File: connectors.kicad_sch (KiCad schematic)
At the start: 0 parts

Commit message: Add RS485 transciever
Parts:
- added J1: 112-024-113R001, Connector_Centronics:CONN_112-024-113R001_NRC, symbol PARTSDB:112-024-113R001
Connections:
- new net GND: J1.18 (Pin_18), J1.19 (Pin_19), J1.20 (Pin_20), J1.21 (Pin_21), J1.22 (Pin_22), J1.23 (Pin_23), J1.24 (Pin_24)

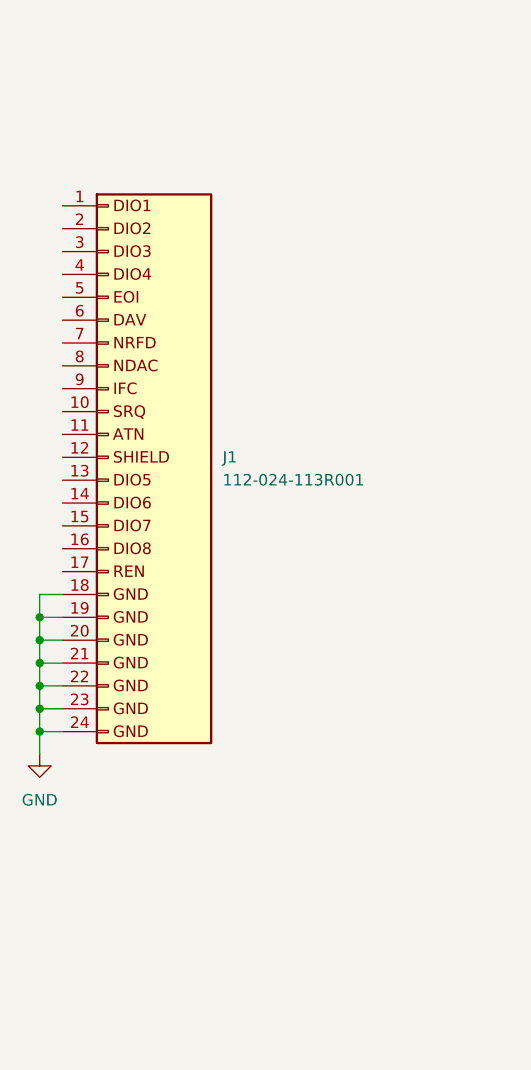
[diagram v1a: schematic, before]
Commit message: Add GPIB and RS485 (CtrlLink) ports
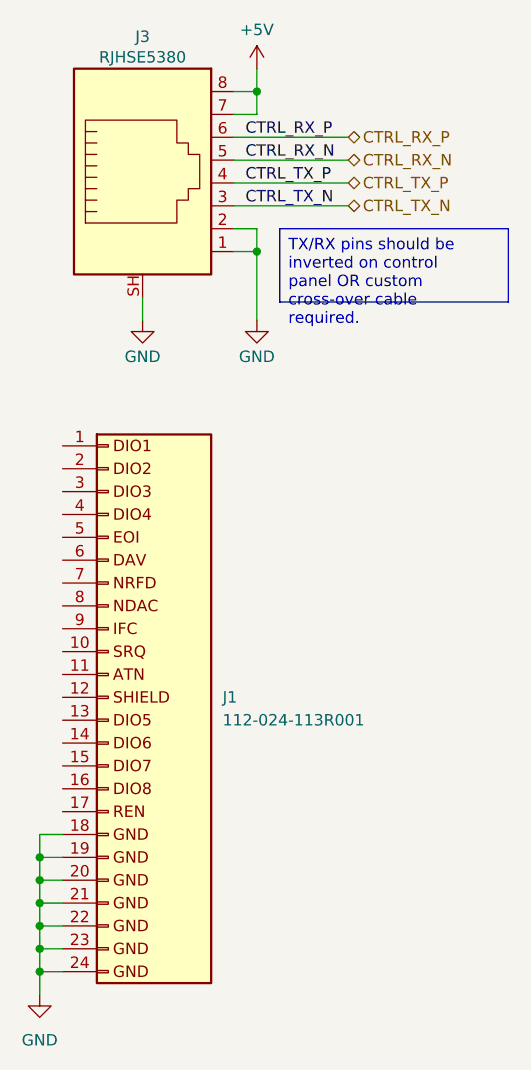
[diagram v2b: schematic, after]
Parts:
- added J3: RJHSE5380, Connector_RJ:RJ45_Amphenol_RJHSE5380, symbol PARTSDB:RJHSE5380
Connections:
- net GND: now also J3.1, J3.2, J3.SH
- new net +5V: J3.7, J3.8
- new net CTRL_RX_N: J3.5
- new net CTRL_RX_P: J3.6
- new net CTRL_TX_N: J3.3
- new net CTRL_TX_P: J3.4
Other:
- moved on the sheet: J1

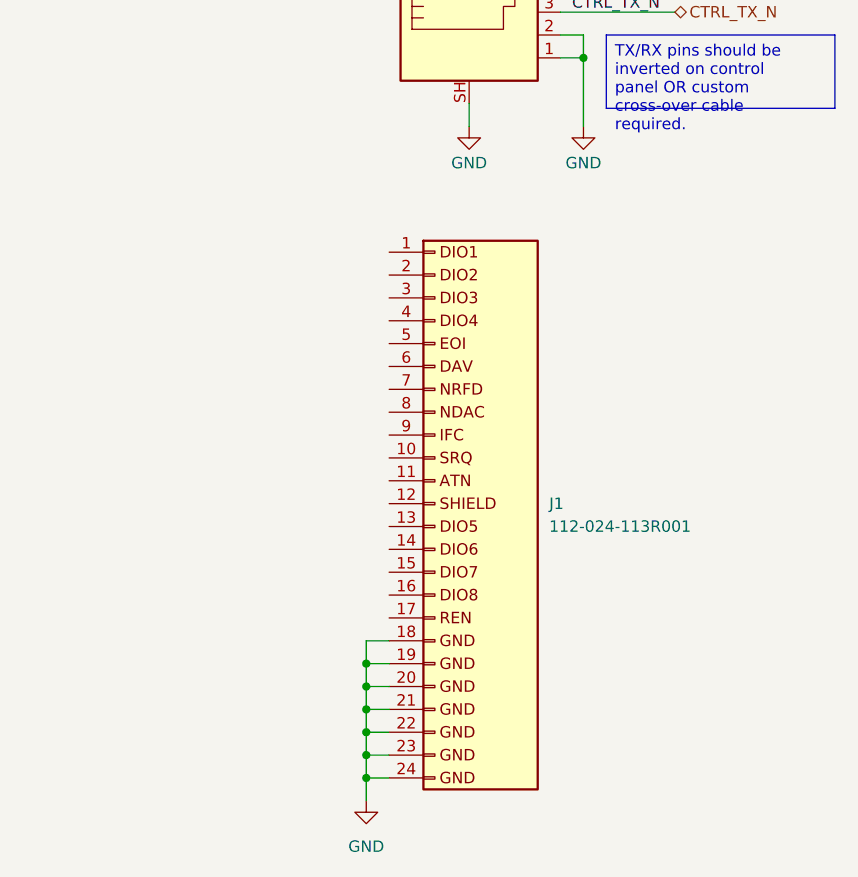
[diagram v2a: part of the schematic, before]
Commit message: Link DIO nets to GPIB connector
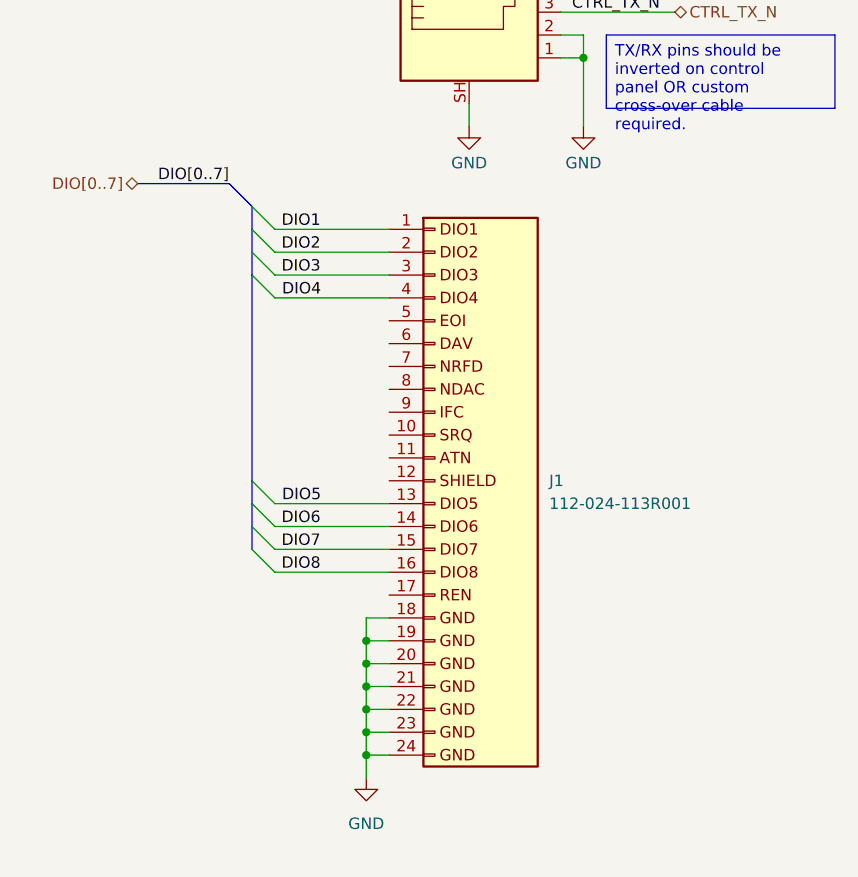
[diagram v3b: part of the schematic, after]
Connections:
- net DIO1: now reaches J1.1 (Pin_1)
- net DIO6: now reaches J1.14 (Pin_14)
- net DIO7: now reaches J1.15 (Pin_15)
- net DIO8: now reaches J1.16 (Pin_16)
- net DIO2: now reaches J1.2 (Pin_2)
- net DIO3: now reaches J1.3 (Pin_3)
- net DIO4: now reaches J1.4 (Pin_4)
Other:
- moved on the sheet: J1

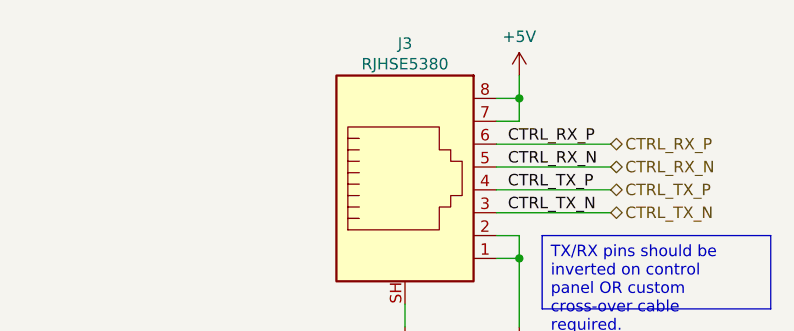
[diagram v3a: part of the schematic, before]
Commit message: Added open-drain driver for GPIB control pins
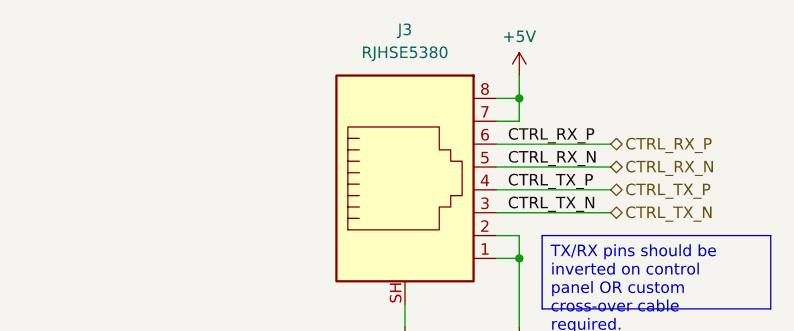
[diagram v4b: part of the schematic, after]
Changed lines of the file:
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@@
+	)
+	(symbol
+		(lib_id "PARTSDB:RJHSE5380")
+		(at 190.5 60.96 0)
+		(unit 1)
+		(body_style 1)
+		(exclude_from_sim no)
+		(in_bom yes)
+		(on_board yes)
+		(in_pos_files yes)
+		(dnp no)
+		(fields_autoplaced yes)
+		(property "Reference" "J3"
+			(at 190.5 43.18 0)
+			(show_name no)
+			(do_not_autoplace no)
+			(effects
+				(font
+					(size 1.27 1.27)
+				)
+			)
+		)
+		(property "Value" "RJHSE5380"
+			(at 190.5 45.72 0)
+			(show_name no)
+			(do_not_autoplace no)
+			(effects
+				(font
+					(size 1.27 1.27)
+				)
+			)
+		)
+		(property "Footprint" "Connector_RJ:RJ45_Amphenol_RJHSE5380"
+			(at 190.5 60.325 90)
+			(hide yes)
+			(show_name no)
+			(do_not_autoplace no)
+			(effects
+				(font
+					(size 1.27 1.27)
+				)
+			)
+		)
+		(property "Datasheet" "https://cdn.amphenol-cs.com/media/wysiwyg/files/documentation/datasheet/inputoutput/io-modjack-rjhse.pdf"
+			(at 190.5 60.325 90)
+			(hide yes)
+			(show_name no)
+			(do_not_autoplace no)
+			(effects
+				(font
+					(size 1.27 1.27)
+				)
+			)
+		)
+		(property "Description" "Jack Modular Connector 8p8c (RJ45, Ethernet) 90° Angle (Right) Shielded, EMI Finger"
+			(at 190.5 60.96 0)
+			(hide yes)
+			(show_name no)
+			(do_not_autoplace no)
+			(effects
+				(font
+					(size 1.27 1.27)
+				)
+			)
+		)
+		(property "Part-DB URL" "http://parts.husbylabs.com/en/part/12/info"
+			(at 190.5 60.96 0)
+			(hide yes)
+			(show_name no)
+			(do_not_autoplace no)
+			(effects
+				(font
+					(size 1.27 1.27)
+				)
+			)
+		)
+		(property "Category" "Connectors, Interconnects/Modular/Ethernet Connectors"
+			(at 190.5 60.96 0)
+			(hide yes)
+			(show_name no)
+			(do_not_autoplace no)
+			(effects
+				(font
+					(size 1.27 1.27)
+				)
+			)
+		)
+		(property "Manufacturer" "Amphenol ICC (Commercial Products)"
+			(at 190.5 60.96 0)
+			(hide yes)
+			(show_name no)
+			(do_not_autoplace no)
+			(effects
+				(font
+					(size 1.27 1.27)
+				)
+			)
+		)
+		(property "MPN" "RJHSE5380"
+			(at 190.5 60.96 0)
+			(hide yes)
+			(show_name no)
+			(do_not_autoplace no)
+			(effects
+				(font
+					(size 1.27 1.27)
+				)
+			)
+		)
+		(property "Manufacturing Status" "Active"
+			(at 190.5 60.96 0)
+			(hide yes)
+			(show_name no)
+			(do_not_autoplace no)
+			(effects
+				(font
+					(size 1.27 1.27)
+				)
+			)
+		)
+		(property "Part-DB ID" "12"
+			(at 190.5 60.96 0)
+			(hide yes)
+			(show_name no)
+			(do_not_autoplace no)
+			(effects
+				(font
+					(size 1.27 1.27)
+				)
+			)
+		)
+		(property "manf" "Amphenol ICC (Commercial Products)"
+			(at 190.5 60.96 0)
+			(hide yes)
+			(show_name no)
+			(do_not_autoplace no)
+			(effects
+				(font
+					(size 1.27 1.27)
+				)
+			)
+		)
+		(property "manf#" "RJHSE5380"
+			(at 190.5 60.96 0)
+			(hide yes)
+			(show_name no)
+			(do_not_autoplace no)
+			(effects
+				(font
+					(size 1.27 1.27)
+				)
+			)
+		)
+		(property "DigiKey SPN" "664-RJHSE5380-ND"
+			(at 190.5 60.96 0)
+			(hide yes)
+			(show_name no)
+			(do_not_autoplace no)
+			(effects
+				(font
+					(size 1.27 1.27)
+				)
+			)
+		)
+		(property "digikey#" "664-RJHSE5380-ND"
+			(at 190.5 60.96 0)
+			(hide yes)
+			(show_name no)
+			(do_not_autoplace no)
+			(effects
+				(font
+					(size 1.27 1.27)
+				)
+			)
+		)
+		(property "Stock" "0"
+			(at 190.5 60.96 0)
+			(hide yes)
+			(show_name no)
+			(do_not_autoplace no)
+			(effects
+				(font
+					(size 1.27 1.27)
+				)
+			)
+		)
+		(pin "7"
+		)
+		(pin "8"
+		)
+		(pin "SH"
+		)
+		(pin "6"
+		)
+		(pin "1"
+		)
+		(pin "2"
+		)
+		(pin "3"
+		)
+		(pin "4"
+		)
+		(pin "5"
+		)
+		(instances
+			(project "gpib_controller"
+				(path "/0f352524-50ff-469d-9a68-783e183b0073/642cbd6b-8c2c-4a8a-b65c-89c798f24c3f/b8b9e038-f19a-4634-b386-ca56990adcb1"
+					(reference "J3")
+					(unit 1)
+				)
+			)
+		)
 	)
 	(symbol
@@
 					(unit 1)
 				)
-			)
-		)
-	)
-	(symbol
-		(lib_id "PARTSDB:RJHSE5380")
-		(at 190.5 60.96 0)
-		(unit 1)
-		(body_style 1)
-		(exclude_from_sim no)
-		(in_bom yes)
-		(on_board yes)
-		(in_pos_files yes)
-		(dnp no)
-		(property "Reference" "J3"
-			(at 190.5 44.704 0)
-			(show_name no)
-			(do_not_autoplace no)
-			(effects
-				(font
-					(size 1.27 1.27)
-				)
-			)
-		)
-		(property "Value" "RJHSE5380"
-			(at 190.5 46.99 0)
-			(show_name no)
-			(do_not_autoplace no)
-			(effects
-				(font
-					(size 1.27 1.27)
-				)
-			)
-		)
-		(property "Footprint" "Connector_RJ:RJ45_Amphenol_RJHSE5380"
-			(at 190.5 60.325 90)
-			(hide yes)
-			(show_name no)
-			(do_not_autoplace no)
-			(effects
-				(font
-					(size 1.27 1.27)
-				)
-			)
-		)
-		(property "Datasheet" "https://cdn.amphenol-cs.com/media/wysiwyg/files/documentation/datasheet/inputoutput/io-modjack-rjhse.pdf"
-			(at 190.5 60.325 90)
-			(hide yes)
-			(show_name no)
-			(do_not_autoplace no)
-			(effects
-				(font
-					(size 1.27 1.27)
-				)
-			)
-		)
-		(property "Description" "Jack Modular Connector 8p8c (RJ45, Ethernet) 90° Angle (Right) Shielded, EMI Finger"
-			(at 190.5 60.96 0)
-			(hide yes)
-			(show_name no)
-			(do_not_autoplace no)
-			(effects
-				(font
-					(size 1.27 1.27)
-				)
-			)
-		)
-		(property "Part-DB URL" "http://parts.husbylabs.com/en/part/12/info"
-			(at 190.5 60.96 0)
-			(hide yes)
-			(show_name no)
-			(do_not_autoplace no)
-			(effects
-				(font
-					(size 1.27 1.27)
-				)
-			)
-		)
-		(property "Category" "Connectors, Interconnects/Modular/Ethernet Connectors"
-			(at 190.5 60.96 0)
-			(hide yes)
-			(show_name no)
-			(do_not_autoplace no)
-			(effects
-				(font
-					(size 1.27 1.27)
-				)
-			)
-		)
-		(property "Manufacturer" "Amphenol ICC (Commercial Products)"
-			(at 190.5 60.96 0)
-			(hide yes)
-			(show_name no)
-			(do_not_autoplace no)
-			(effects
-				(font
-					(size 1.27 1.27)
-				)
-			)
-		)
-		(property "MPN" "RJHSE5380"
-			(at 190.5 60.96 0)
-			(hide yes)
-			(show_name no)
-			(do_not_autoplace no)
-			(effects
-				(font
-					(size 1.27 1.27)
-				)
-			)
-		)
-		(property "Manufacturing Status" "Active"
-			(at 190.5 60.96 0)
-			(hide yes)
-			(show_name no)
-			(do_not_autoplace no)
-			(effects
-				(font
-					(size 1.27 1.27)
-				)
-			)
-		)
-		(property "Part-DB ID" "12"
-			(at 190.5 60.96 0)
-			(hide yes)
-			(show_name no)
-			(do_not_autoplace no)
-			(effects
-				(font
-					(size 1.27 1.27)
-				)
-			)
-		)
-		(property "manf" "Amphenol ICC (Commercial Products)"
-			(at 190.5 60.96 0)
-			(hide yes)
-			(show_name no)
-			(do_not_autoplace no)
-			(effects
-				(font
-					(size 1.27 1.27)
-				)
-			)
-		)
-		(property "manf#" "RJHSE5380"
-			(at 190.5 60.96 0)
-			(hide yes)
-			(show_name no)
-			(do_not_autoplace no)
-			(effects
-				(font
-					(size 1.27 1.27)
-				)
-			)
-		)
-		(property "DigiKey SPN" "664-RJHSE5380-ND"
-			(at 190.5 60.96 0)
-			(hide yes)
-			(show_name no)
-			(do_not_autoplace no)
-			(effects
-				(font
-					(size 1.27 1.27)
-				)
-			)
-		)
-		(property "digikey#" "664-RJHSE5380-ND"
-			(at 190.5 60.96 0)
-			(hide yes)
-			(show_name no)
-			(do_not_autoplace no)
-			(effects
-				(font
-					(size 1.27 1.27)
-				)
-			)
-		)
-		(property "Stock" "0"
-			(at 190.5 60.96 0)
-			(hide yes)
-			(show_name no)
-			(do_not_autoplace no)
-			(effects
-				(font
-					(size 1.27 1.27)
-				)
-			)
-		)
-		(pin "6"
-		)
-		(pin "5"
-		)
-		(pin "4"
-		)
-		(pin "3"
-		)
-		(pin "1"
-		)
-		(pin "8"
-		)
-		(pin "7"
-		)
-		(pin "SH"
-		)
-		(pin "2"
-		)
-		(instances
-			(project "gpib_controller"
-				(path "/0f352524-50ff-469d-9a68-783e183b0073/642cbd6b-8c2c-4a8a-b65c-89c798f24c3f/b8b9e038-f19a-4634-b386-ca56990adcb1"
-					(reference "J3")
-					(unit 1)
-				)

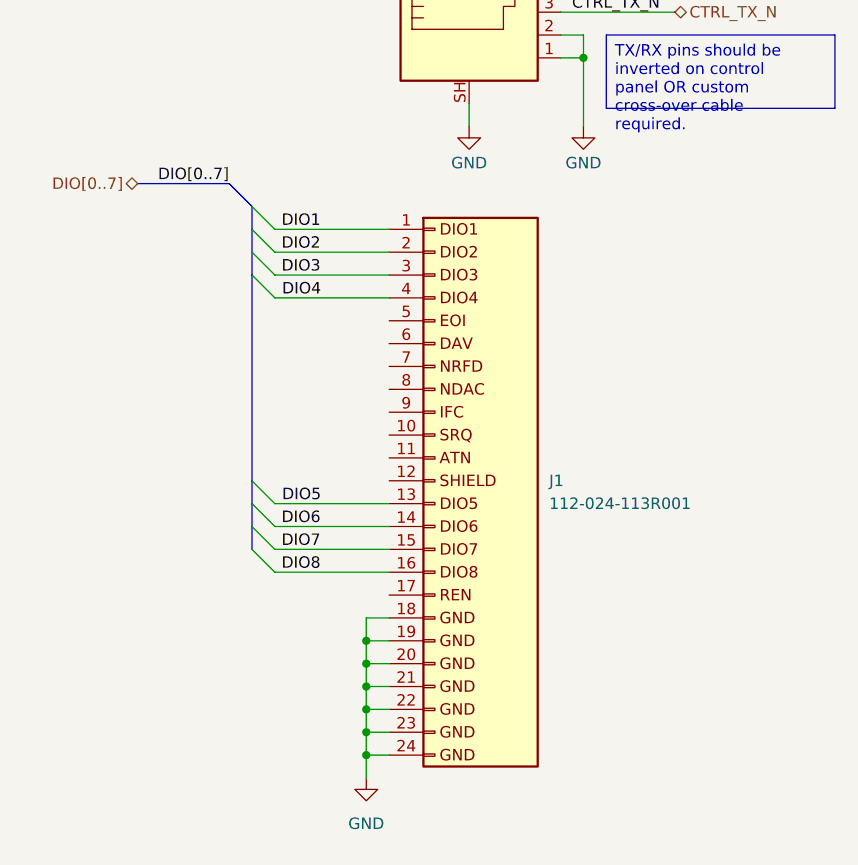
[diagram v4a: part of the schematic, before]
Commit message: Add Schmitt-Trig sense IC, connect GPIB conn nets and run jobfile
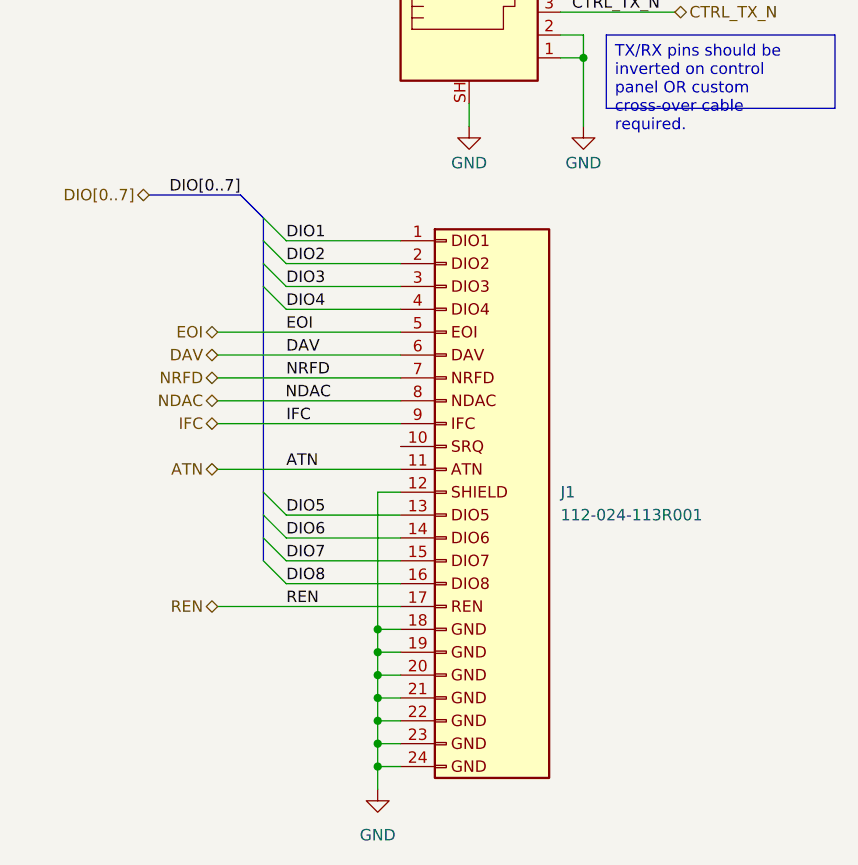
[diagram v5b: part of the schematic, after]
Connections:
- net GND: now also J1.12 (Pin_12)
- net ATN: now reaches J1.11 (Pin_11)
- net REN: now reaches J1.17 (Pin_17)
- net EOI: now reaches J1.5 (Pin_5)
- net DAV: now reaches J1.6 (Pin_6)
- net NRFD: now reaches J1.7 (Pin_7)
- net NDAC: now reaches J1.8 (Pin_8)
- net IFC: now reaches J1.9 (Pin_9)
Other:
- moved on the sheet: J1

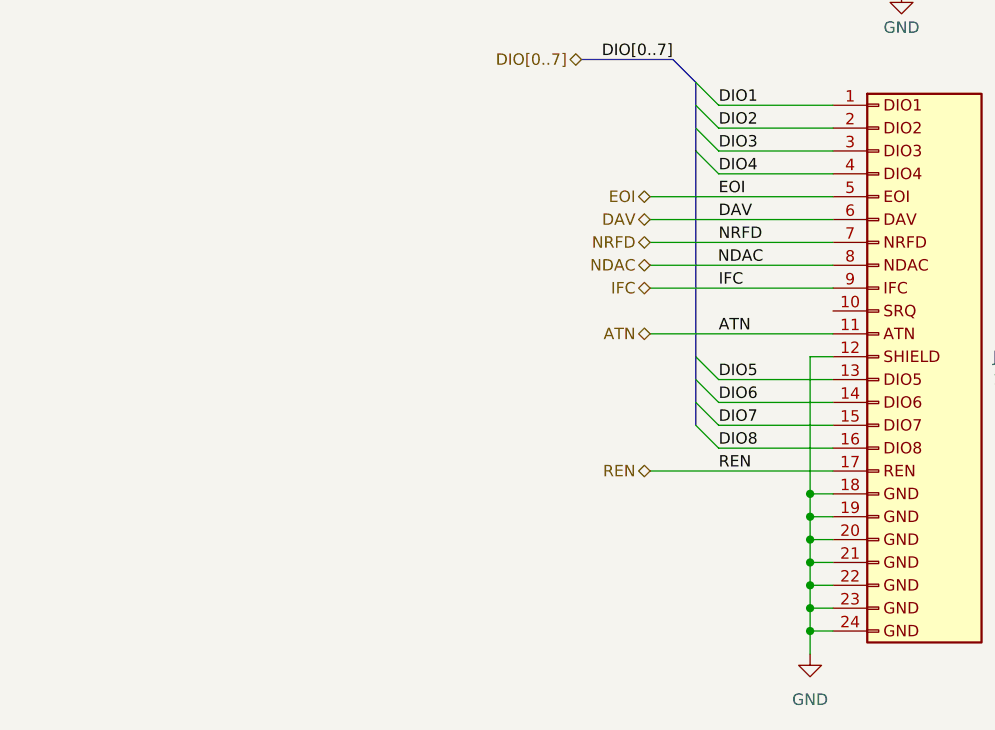
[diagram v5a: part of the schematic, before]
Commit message: Add GPIB interface
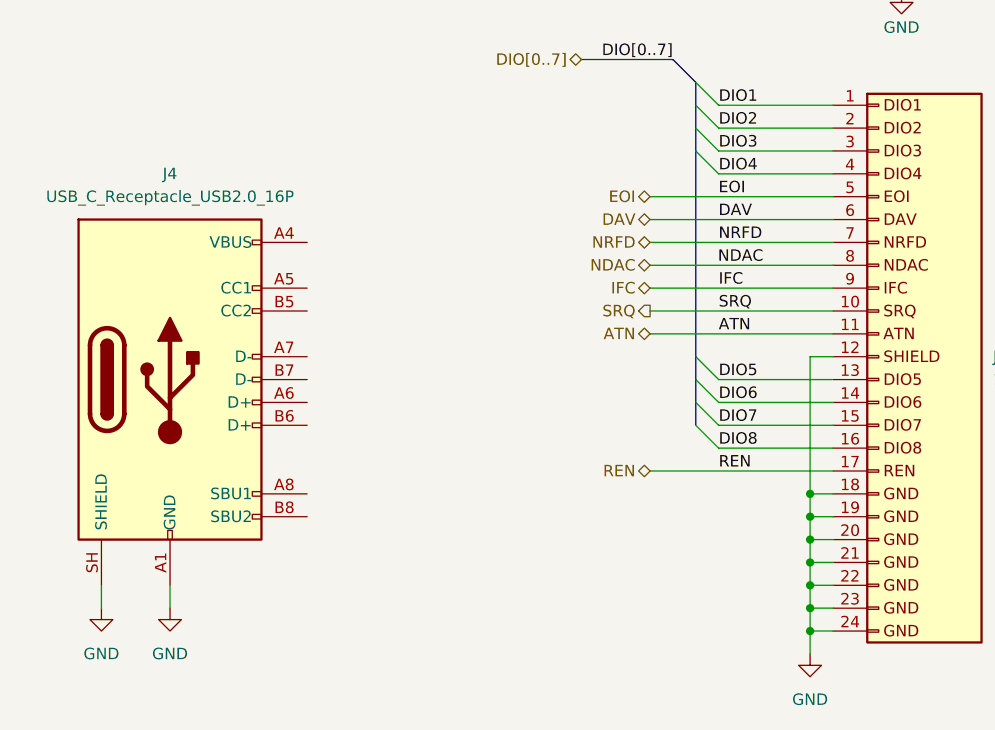
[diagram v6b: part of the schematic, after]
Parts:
- added J4: USB_C_Receptacle_USB2.0_16P, Connector_USB:USB_C_Receptacle_Amphenol_12401948E412A, symbol Connector:USB_C_Receptacle_USB2.0_16P
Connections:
- net GND: now also J4.A1 (GND), J4.A12 (GND), J4.B1 (GND), J4.B12 (GND), J4.SH (SHIELD)
- net SRQ: now reaches J1.10 (Pin_10)
- new net: J4.A4 (VBUS), J4.A9 (VBUS), J4.B4 (VBUS), J4.B9 (VBUS)
